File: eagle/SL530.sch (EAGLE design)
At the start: 42 parts, among them IC4 74LVC1G17DBV, IC5 74LVC1G17DBV, U1 LM1117, X1 MC68000

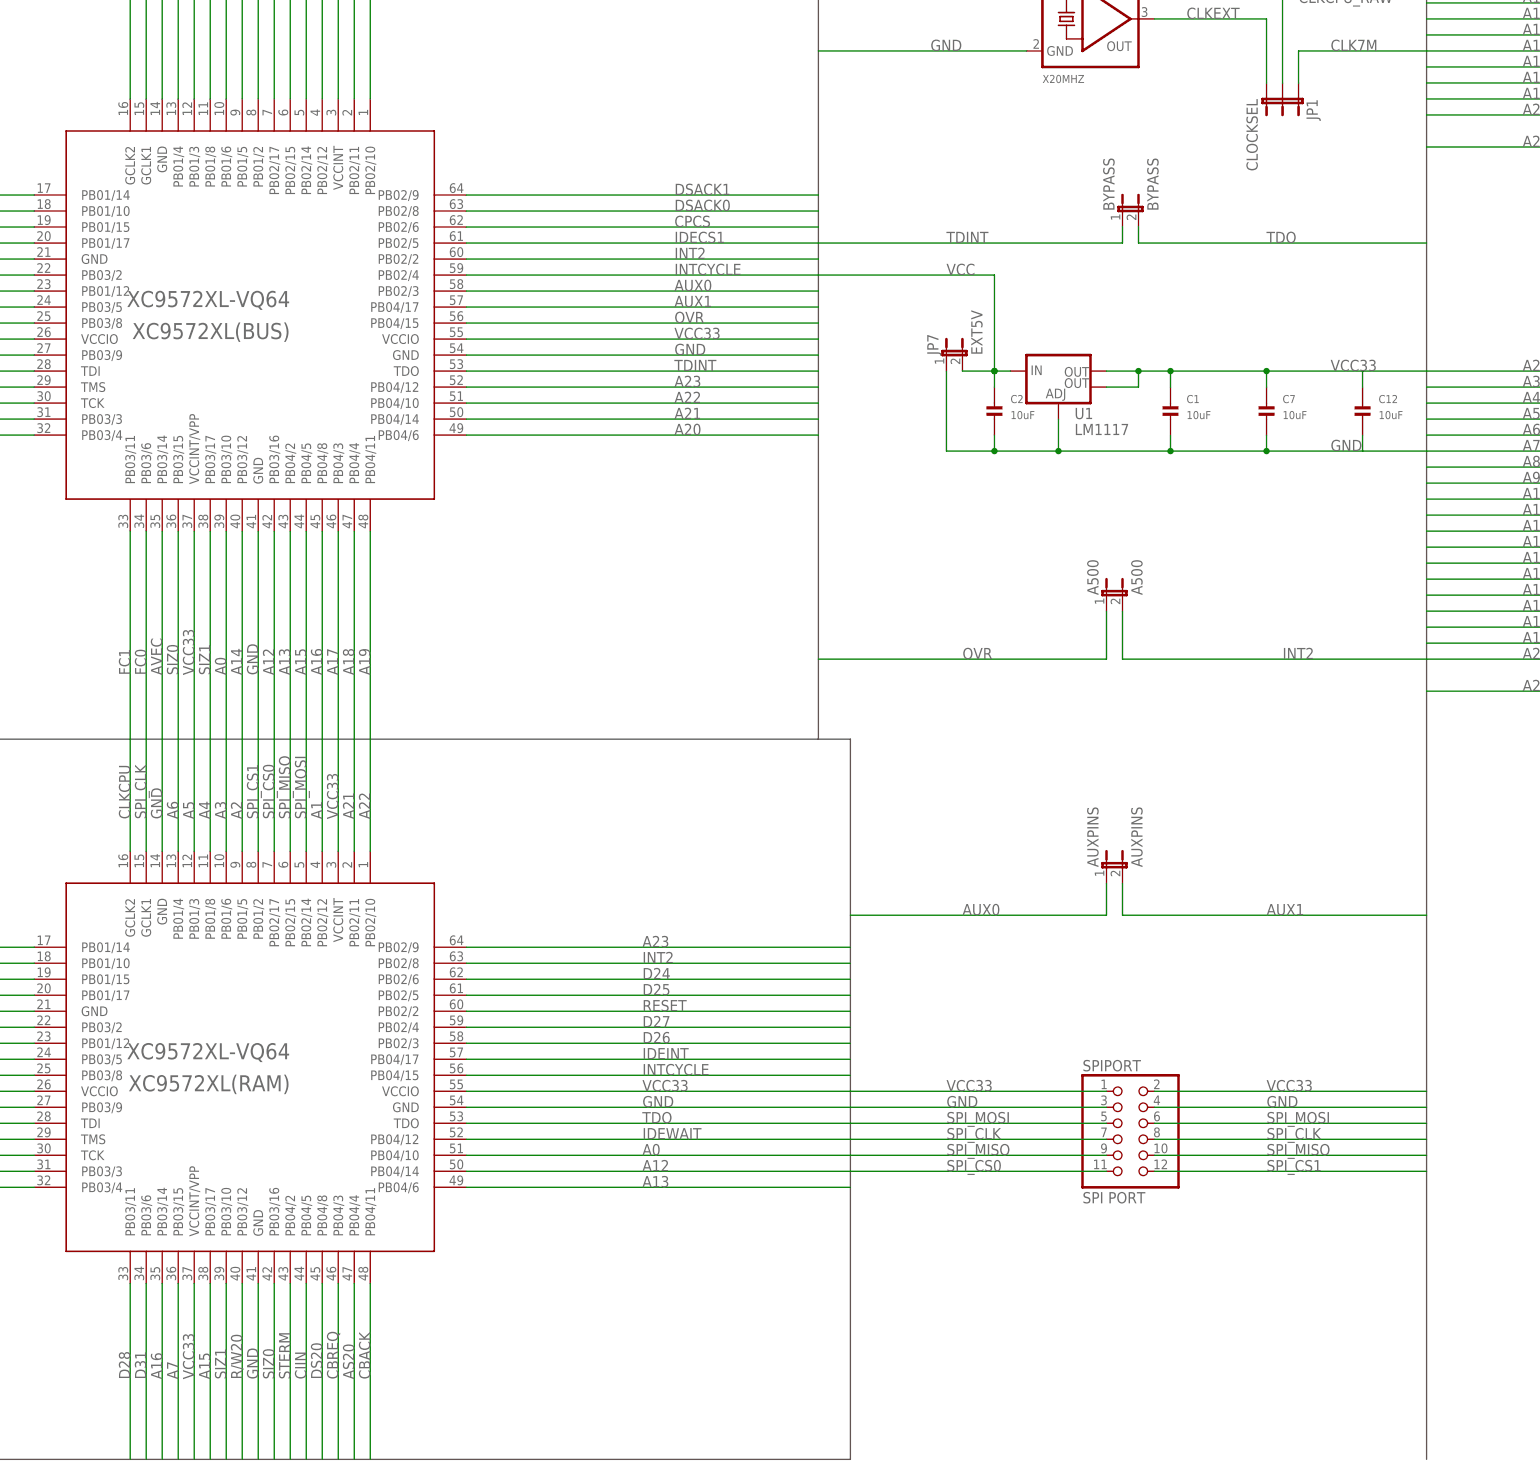
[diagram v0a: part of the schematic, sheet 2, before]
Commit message: Modifications to the TF530. upgrade to eagle 8. Added IPL lines to the bus CPLD. Significant re-routing of the Bus CPLD traces. Incremented version to revision 3 Beefed up power rails. improved routing over the bus cpld. better ground planes.
No CPLD updates yet.. to follow.
Added 2 more decoupling caps for the 030
Removed unused DSACK1/A14/AUX0/AUX1

I have left in OVR and INT2 for test purposes.
These shouldn't need connected.

removed the test traces for A14
removed A7 from the RAM cpld and created a single header pin. potentially for SPI Interrupts (Active HIGH).

Verified pass the DRC checks.
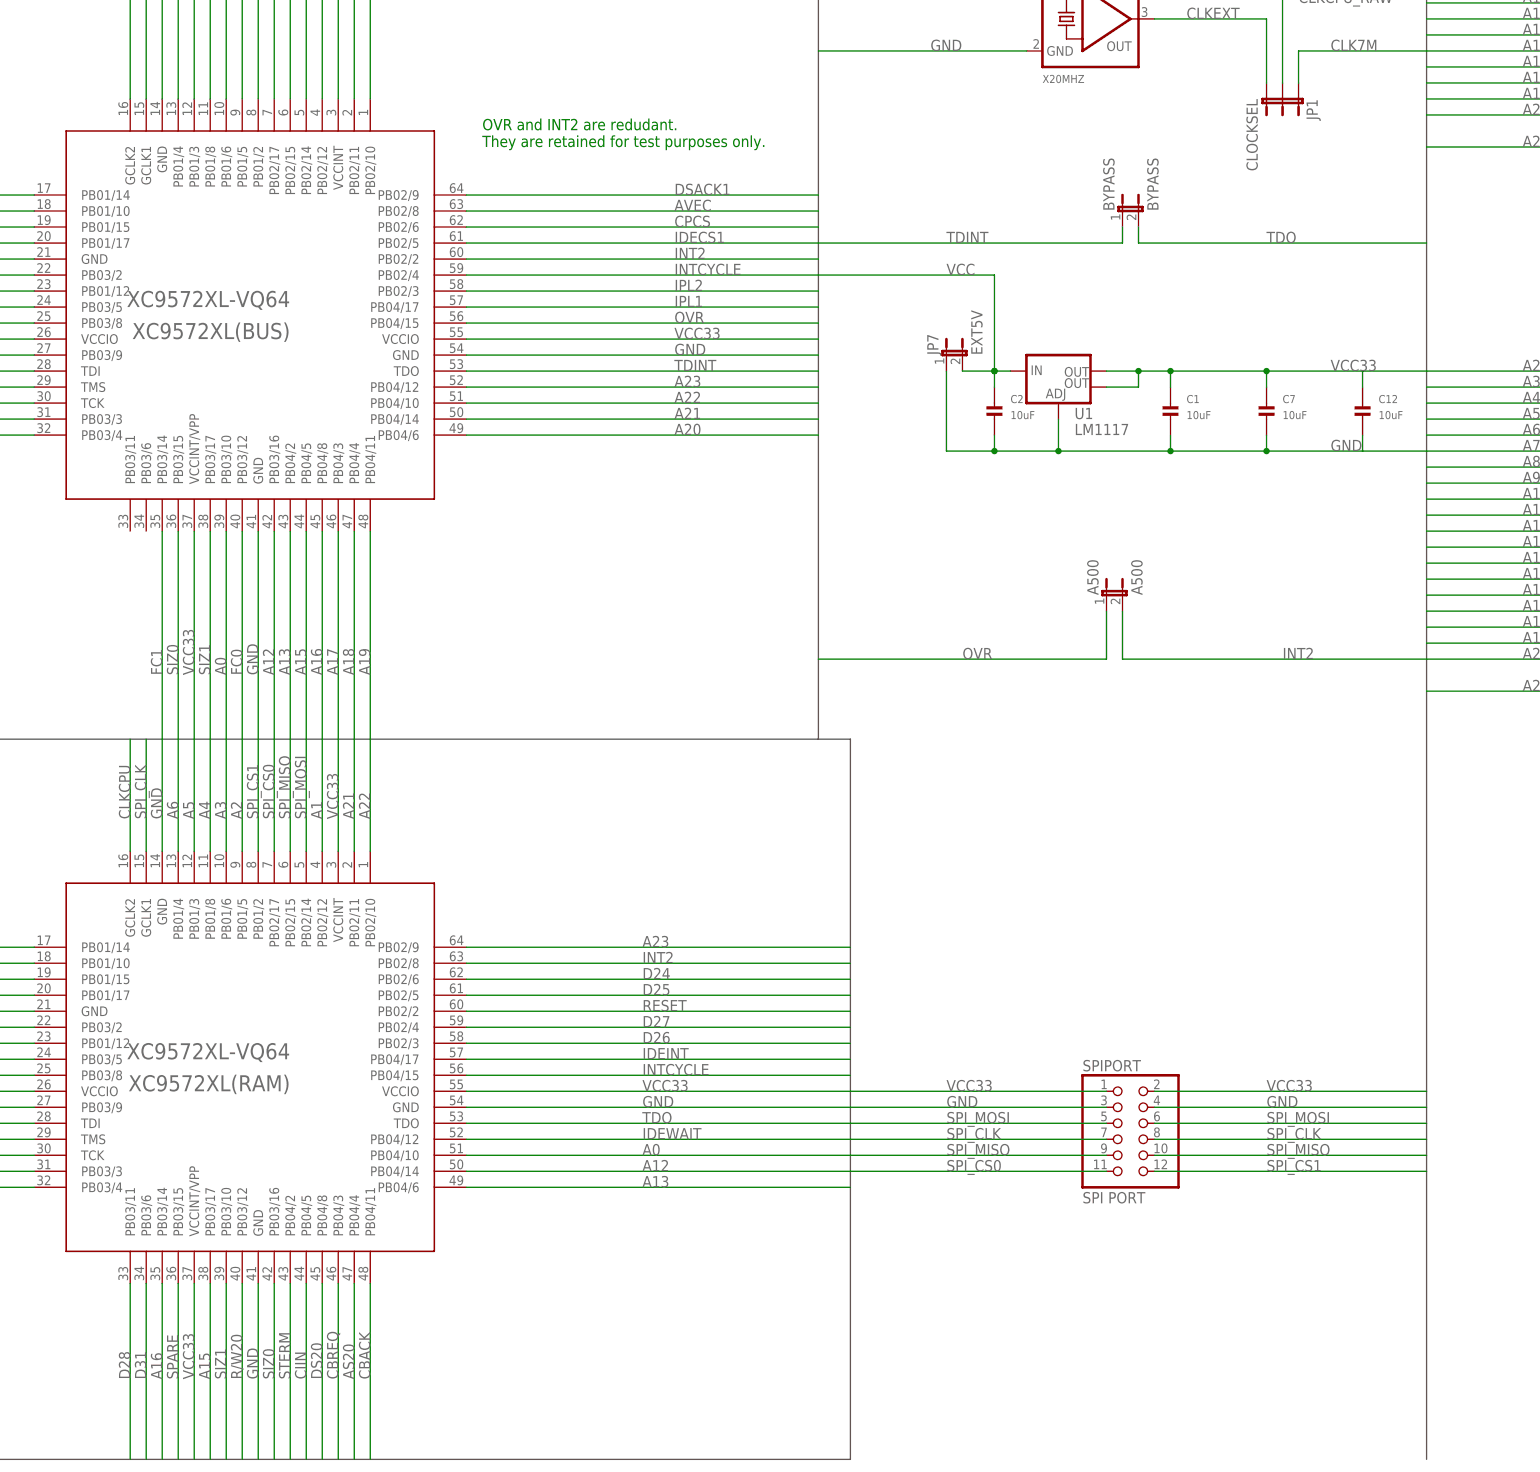
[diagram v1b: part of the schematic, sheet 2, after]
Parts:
- removed AUXPINS: AUXPINS, SparkFun-Retired:JUMPER-2PTH
- added C14, C15: 10uF, microbuilder:CAP_CERAMIC1206
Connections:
- removed net AUX0: AUXPINS.1, XC9572XL(BUS).PB02/3
- removed net AUX1: AUXPINS.2, XC9572XL(BUS).PB04/17
- new net SPARE: XC9572XL(RAM).PB03/15
- net A14: no longer XC9572XL(BUS).PB03/12
- net A7: no longer XC9572XL(RAM).PB03/15
- net AVEC: now also XC9572XL(BUS).PB02/8; no longer XC9572XL(BUS).PB03/14
- net DSACK0: no longer XC9572XL(BUS).PB02/8
- net FC0: now also XC9572XL(BUS).PB03/12; no longer XC9572XL(BUS).PB03/6
- net FC1: now also XC9572XL(BUS).PB03/14; no longer XC9572XL(BUS).PB03/11
- net GND: now also C14.P$2, C15.P$2
- net IPL1: now also XC9572XL(BUS).PB04/17
- net IPL2: now also XC9572XL(BUS).PB02/3
- net VCC: now also C14.P$1, C15.P$1
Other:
- note added: "OVR and INT2 are redudant. They are retained for test purposes only."
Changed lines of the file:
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@@
 <?xml version="1.0" encoding="utf-8"?>
 <!DOCTYPE eagle SYSTEM "eagle.dtd">
-<eagle version="7.7.0">
+<eagle version="8.1.1">
 <drawing>
 <settings>
@@
 <part name="R1" library="microbuilder" deviceset="RESISTOR" device="1206" value="47K"/>
 <part name="R2" library="microbuilder" deviceset="RESISTOR" device="1206" value="47K"/>
-<part name="AUXPINS" library="SparkFun-Retired" deviceset="JUMPER-2" device="PTH" value="AUXPINS"/>
+<part name="C14" library="microbuilder" deviceset="CAP_CERAMIC" device="1206" value="10uF"/>
+<part name="C15" library="microbuilder" deviceset="CAP_CERAMIC" device="1206" value="10uF"/>
 </parts>
 <sheets>
@@
 <instance part="R1" gate="G$1" x="467.36" y="73.66" rot="R180"/>
 <instance part="R2" gate="G$1" x="467.36" y="66.04" rot="R180"/>
+<instance part="C14" gate="G$1" x="535.94" y="195.58"/>
+<instance part="C15" gate="G$1" x="543.56" y="195.58"/>
 </instances>
 <busses>
-<bus name="VCC33,VCC,GND,CLK7M,A[0..31],D[0..31],IPL[0..2],FC[0..2],DSACK[0..1],BR,BGACK,R/W20,R/W,CLKCPU,AS20,DS20,BG20,AVEC,SIZ[0..1],DBEN,BERR,RESET,HALT,BG,VPA,VMA,E,AS,UDS,LDS,DTACK,CPCS,CPSENSE,CDIS,MMUDIS,IOR,IOW,INT2,IDECS[0..1],IDELED,IDEWAIT,IDEINT,RAMOE,RAMCS[0..3],INTSIG[0..4],TCK,TMS,TDI,TDO,TDINT,OVL,CIIN,CIIOUT,CBREQ,CBACK,STERM,STATUS,REFILL,SPI_MOSI,SPI_MISO,SPI_CLK,SPI_CS[0..1],UNDECIDED">
+<bus name="VCC33,VCC,GND,CLK7M,A[0..31],D[0..31],IPL[0..2],FC[0..2],DSACK[0..1],BR,BGACK,R/W20,R/W,CLKCPU,AS20,DS20,BG20,AVEC,SIZ[0..1],DBEN,BERR,RESET,HALT,BG,VPA,VMA,E,AS,UDS,LDS,DTACK,CPCS,CPSENSE,CDIS,MMUDIS,IOR,IOW,INT2,IDECS[0..1],IDELED,IDEWAIT,IDEINT,RAMOE,RAMCS[0..3],INTSIG[0..4],TCK,TMS,TDI,TDO,TDINT,OVL,CIIN,CIIOUT,CBREQ,CBACK,STERM,STATUS,REFILL,SPI_MOSI,SPI_MISO,SPI_CLK,SPI_CS[0..1],SPARE">
 <segment>
 <wire x1="210.82" y1="-5.08" x2="210.82" y2="218.44" width="0.762" layer="92"/>
@@
 <pinref part="C4" gate="G$1" pin="P$2"/>
 <wire x1="454.66" y1="193.04" x2="454.66" y2="182.88" width="0.1524" layer="91"/>
+<pinref part="C14" gate="G$1" pin="P$2"/>
+<wire x1="528.32" y1="182.88" x2="535.94" y2="182.88" width="0.1524" layer="91"/>
+<wire x1="535.94" y1="182.88" x2="535.94" y2="193.04" width="0.1524" layer="91"/>
+<pinref part="C15" gate="G$1" pin="P$2"/>
+<wire x1="535.94" y1="182.88" x2="543.56" y2="182.88" width="0.1524" layer="91"/>
+<wire x1="543.56" y1="182.88" x2="543.56" y2="193.04" width="0.1524" layer="91"/>
 </segment>
 <segment>
@@
 <pinref part="C4" gate="G$1" pin="P$1"/>
 <wire x1="454.66" y1="210.82" x2="454.66" y2="200.66" width="0.1524" layer="91"/>
+<pinref part="C14" gate="G$1" pin="P$1"/>
+<wire x1="528.32" y1="210.82" x2="535.94" y2="210.82" width="0.1524" layer="91"/>
+<wire x1="535.94" y1="210.82" x2="535.94" y2="200.66" width="0.1524" layer="91"/>
+<pinref part="C15" gate="G$1" pin="P$1"/>
+<wire x1="535.94" y1="210.82" x2="543.56" y2="210.82" width="0.1524" layer="91"/>
+<wire x1="543.56" y1="210.82" x2="543.56" y2="200.66" width="0.1524" layer="91"/>
 </segment>
 <segment>
@@
 <sheet>
 <plain>
+<text x="142.24" y="114.3" size="1.778" layer="91">OVR and INT2 are redudant.
+They are retained for test purposes only.</text>
 </plain>
 <instances>
@@
 <instance part="C12" gate="G$1" x="281.94" y="71.12"/>
 <instance part="SPIPORT" gate="A" x="243.84" y="-40.64"/>
-<instance part="AUXPINS" gate="A" x="241.3" y="0"/>
 </instances>
 <busses>
-<bus name="VCC33,VCC,GND,CLK7M,A[0..31],D[0..31],IPL[0..2],FC[0..2],DSACK[0..1],BR,BGACK,R/W20,R/W,CLKCPU,AS20,DS20,BG20,AVEC,SIZ[0..1],DBEN,BERR,RESET,HALT,BG,VPA,VMA,E,AS,UDS,LDS,DTACK,CPCS,CPSENSE,CDIS,MMUDIS,IOR,IOW,INT2,IDECS[0..1],IDELED,IDEWAIT,IDEINT,RAMOE,RAMCS[0..3],INTSIG[0..4],TCK,TMS,TDI,TDO,TDINT,OVL,CIIN,CIIOUT,CBREQ,CBACK,STERM,STATUS,REFILL,SPI_MOSI,SPI_MISO,SPI_CLK,SPI_CS[0..1],AUX[0..1]">
+<bus name="VCC33,VCC,GND,CLK7M,A[0..31],D[0..31],IPL[0..2],FC[0..2],DSACK[0..1],BR,BGACK,R/W20,R/W,CLKCPU,AS20,DS20,BG20,AVEC,SIZ[0..1],DBEN,BERR,RESET,HALT,BG,VPA,VMA,E,AS,UDS,LDS,DTACK,CPCS,CPSENSE,CDIS,MMUDIS,IOR,IOW,INT2,IDECS[0..1],IDELED,IDEWAIT,IDEINT,RAMOE,RAMCS[0..3],INTSIG[0..4],TCK,TMS,TDI,TDO,TDINT,OVL,CIIN,CIIOUT,CBREQ,CBACK,STERM,STATUS,REFILL,SPI_MOSI,SPI_MISO,SPI_CLK,SPI_CS[0..1],SPARE">
 <segment>
 <wire x1="12.7" y1="180.34" x2="12.7" y2="20.32" width="0.762" layer="92"/>
@@
 </segment>
 </net>
-<net name="DSACK0" class="0">
-<segment>
-<pinref part="XC9572XL(BUS)" gate="XC9572XL-VQ64" pin="PB02/8"/>
-<wire x1="195.58" y1="104.14" x2="139.7" y2="104.14" width="0.1524" layer="91"/>
-<label x="172.72" y="104.14" size="1.778" layer="95"/>
-</segment>
-</net>
 <net name="A2" class="0">
 <segment>
@@
 <pinref part="U$2" gate="G$1" pin="A5"/>
 </segment>
-<segment>
-<pinref part="XC9572XL(RAM)" gate="XC9572XL-VQ64" pin="PB03/15"/>
-<wire x1="93.98" y1="-93.98" x2="93.98" y2="-66.04" width="0.1524" layer="91"/>
-<label x="93.98" y="-81.28" size="1.778" layer="95" rot="R90"/>
-</segment>
 </net>
 <net name="A8" class="0">
@@
 <pinref part="U$2" gate="G$1" pin="A12"/>
 </segment>
-<segment>
-<pinref part="XC9572XL(BUS)" gate="XC9572XL-VQ64" pin="PB03/12"/>
-<wire x1="104.14" y1="20.32" x2="104.14" y2="53.34" width="0.1524" layer="91"/>
-<label x="104.14" y="30.48" size="1.778" layer="95" rot="R90"/>
-</segment>
 </net>
 <net name="A15" class="0">
@@
 </segment>
 </net>
-<net name="AVEC" class="0">
-<segment>
-<pinref part="XC9572XL(BUS)" gate="XC9572XL-VQ64" pin="PB03/14"/>
-<wire x1="91.44" y1="20.32" x2="91.44" y2="53.34" width="0.1524" layer="91"/>
-<label x="91.44" y="30.48" size="1.778" layer="95" rot="R90"/>
-</segment>
-</net>
 <net name="FC0" class="0">
 <segment>
-<wire x1="88.9" y1="20.32" x2="88.9" y2="53.34" width="0.1524" layer="91"/>
-<pinref part="XC9572XL(BUS)" gate="XC9572XL-VQ64" pin="PB03/6"/>
-<label x="88.9" y="30.48" size="1.778" layer="95" rot="R90"/>
-</segment>
-</net>
-<net name="FC1" class="0">
-<segment>
-<pinref part="XC9572XL(BUS)" gate="XC9572XL-VQ64" pin="PB03/11"/>
-<wire x1="86.36" y1="20.32" x2="86.36" y2="53.34" width="0.1524" layer="91"/>
-<label x="86.36" y="30.48" size="1.778" layer="95" rot="R90"/>
+<pinref part="XC9572XL(BUS)" gate="XC9572XL-VQ64" pin="PB03/12"/>
+<wire x1="104.14" y1="20.32" x2="104.14" y2="53.34" width="0.1524" layer="91"/>
+<label x="104.14" y="30.48" size="1.778" layer="95" rot="R90"/>
 </segment>
 </net>
@@
 </segment>
 </net>
-<net name="AUX0" class="0">
+<net name="IPL2" class="0">
 <segment>
 <pinref part="XC9572XL(BUS)" gate="XC9572XL-VQ64" pin="PB02/3"/>
@@
 <label x="172.72" y="91.44" size="1.778" layer="95"/>
 </segment>
-<segment>
-<pinref part="AUXPINS" gate="A" pin="1"/>
-<wire x1="200.66" y1="-7.62" x2="241.3" y2="-7.62" width="0.1524" layer="91"/>
-<wire x1="241.3" y1="-7.62" x2="241.3" y2="-2.54" width="0.1524" layer="91"/>
-<label x="218.44" y="-7.62" size="1.778" layer="95"/>
-</segment>
 </net>
-<net name="AUX1" class="0">
+<net name="IPL1" class="0">
 <segment>
 <pinref part="XC9572XL(BUS)" gate="XC9572XL-VQ64" pin="PB04/17"/>
@@
 <label x="172.72" y="88.9" size="1.778" layer="95"/>
 </segment>
+</net>
+<net name="AVEC" class="0">
+<segment>
+<pinref part="XC9572XL(BUS)" gate="XC9572XL-VQ64" pin="PB02/8"/>
+<wire x1="195.58" y1="104.14" x2="139.7" y2="104.14" width="0.1524" layer="91"/>
+<label x="172.72" y="104.14" size="1.778" layer="95"/>
+</segment>
+</net>
+<net name="FC1" class="0">
 <segment>
-<pinref part="AUXPINS" gate="A" pin="2"/>
-<wire x1="292.1" y1="-7.62" x2="243.84" y2="-7.62" width="0.1524" layer="91"/>
-<wire x1="243.84" y1="-7.62" x2="243.84" y2="-2.54" width="0.1524" layer="91"/>
-<label x="266.7" y="-7.62" size="1.778" layer="95"/>
+<pinref part="XC9572XL(BUS)" gate="XC9572XL-VQ64" pin="PB03/14"/>
+<wire x1="91.44" y1="20.32" x2="91.44" y2="53.34" width="0.1524" layer="91"/>
+<label x="91.44" y="30.48" size="1.778" layer="95" rot="R90"/>
+</segment>
+</net>
+<net name="SPARE" class="0">
+<segment>
+<pinref part="XC9572XL(RAM)" gate="XC9572XL-VQ64" pin="PB03/15"/>
+<wire x1="93.98" y1="-93.98" x2="93.98" y2="-66.04" width="0.1524" layer="91"/>
+<label x="93.98" y="-81.28" size="1.778" layer="95" rot="R90"/>
 </segment>
 </net>
@@
 </schematic>
 </drawing>
+<compatibility>
+<note version="6.3" minversion="6.2.2" severity="warning">
+Since Version 6.2.2 text objects can contain more than one line,
+which will not be processed correctly with this version.
+</note>
+</compatibility>
 </eagle>

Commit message: Bit of a clean up of the silkscreen Really beefed up VCC to the CPU more ground beefing added an experimental (optional) resistor to load the CPU clock line. added 2 more 0603 caps. One for the CPU and one for the FPU. This version was submitted to dirtypcsb as revision 3
Bit more tidy up on the routing around the bus cpld.
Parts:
- added C16, C17: 0.1uF, SparkFun-Capacitors:0.1UF-25V(+80/-20%)(0603)
- added RCLKLOAD: INF, SparkFun-Resistors:0.05OHM-1/5W-1%(0603)
- IC3: value LM1117 -> LM1117-3.3
- R3: value 10K -> 47K
- TP1: value A500 -> TP1
- renumbered A500 to TP1, IDE to IDECONNECTOR, JP7 to PWR1, U$1 to IC8, U$2 to IC6, U$3 to IC7, U$4 to IC9, U1 to IC3
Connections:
- net CLKCPU: now also RCLKLOAD.1
- net GND: now also C16.2, C17.2, RCLKLOAD.2
- net VCC: now also C16.1, C17.1
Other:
- note added: "C14-C17 are for tuning/stability purposes. These should not be required for normal operation but can be used to help with instability."
- note added: "Terrible Fire TF530 Revision 3 Copyright (C) 2017 Stephen J. Leary All Rights Reserved."
- note added: "This is now a test point. No longer required for standard operation."
- note added: "This resistor is to let me experiment with clock line loads to tune to higher clock frequencies. It is not required for 24Mhz operation"
- note added: "Without these resistor networks the control bus floats low and does not work."
